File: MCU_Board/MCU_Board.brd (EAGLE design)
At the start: 88 x 41 mm, 81 parts, among them J1 22-05-7068-06, J10 22-05-7068-06, J11 22-05-7048-04, J12 22-27-2061-06, J13 USB3075-30-A, J14 22-05-7048-04, J15 1241050-5, J2 22-05-7068-06, J3 22-05-7028-02, J4 22-05-7028-02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

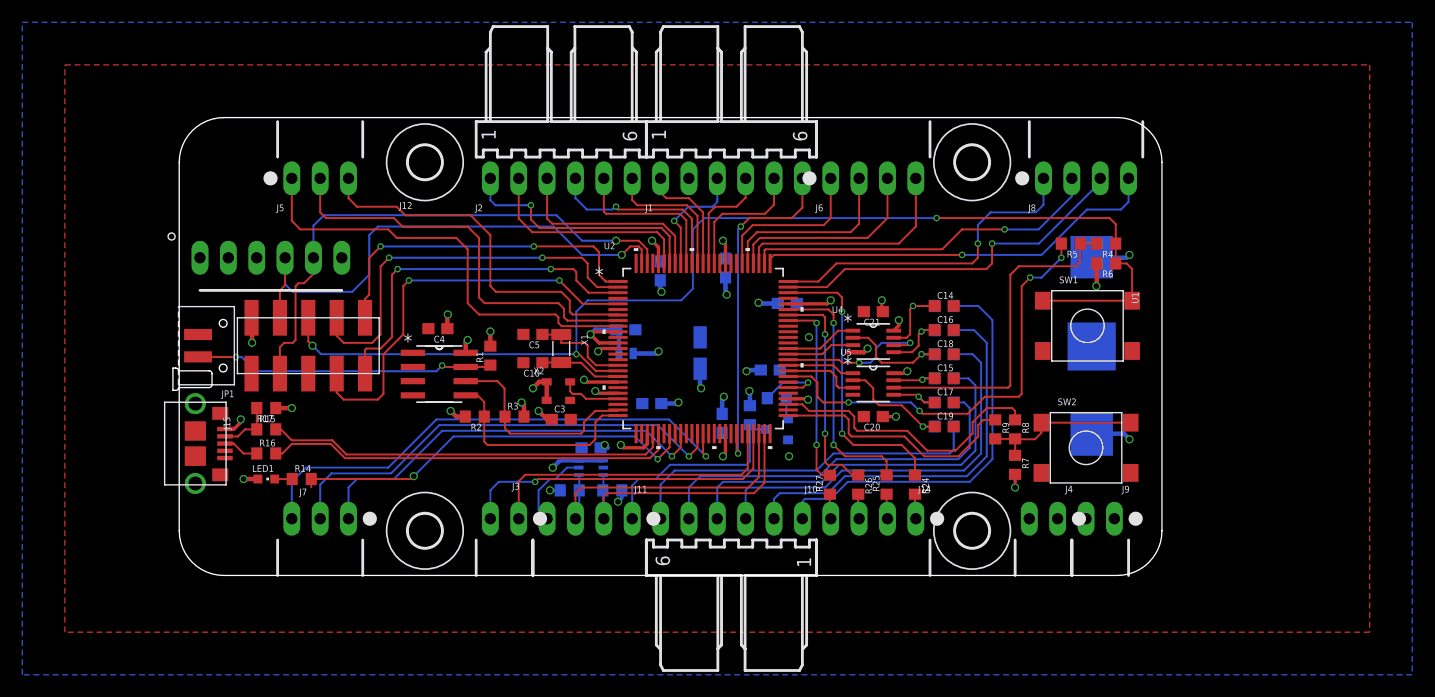
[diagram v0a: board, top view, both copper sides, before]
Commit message: Add limitation resistance on Encoder output, ADC input, relay input and fan Add LED on board Poly for +5V on Route15
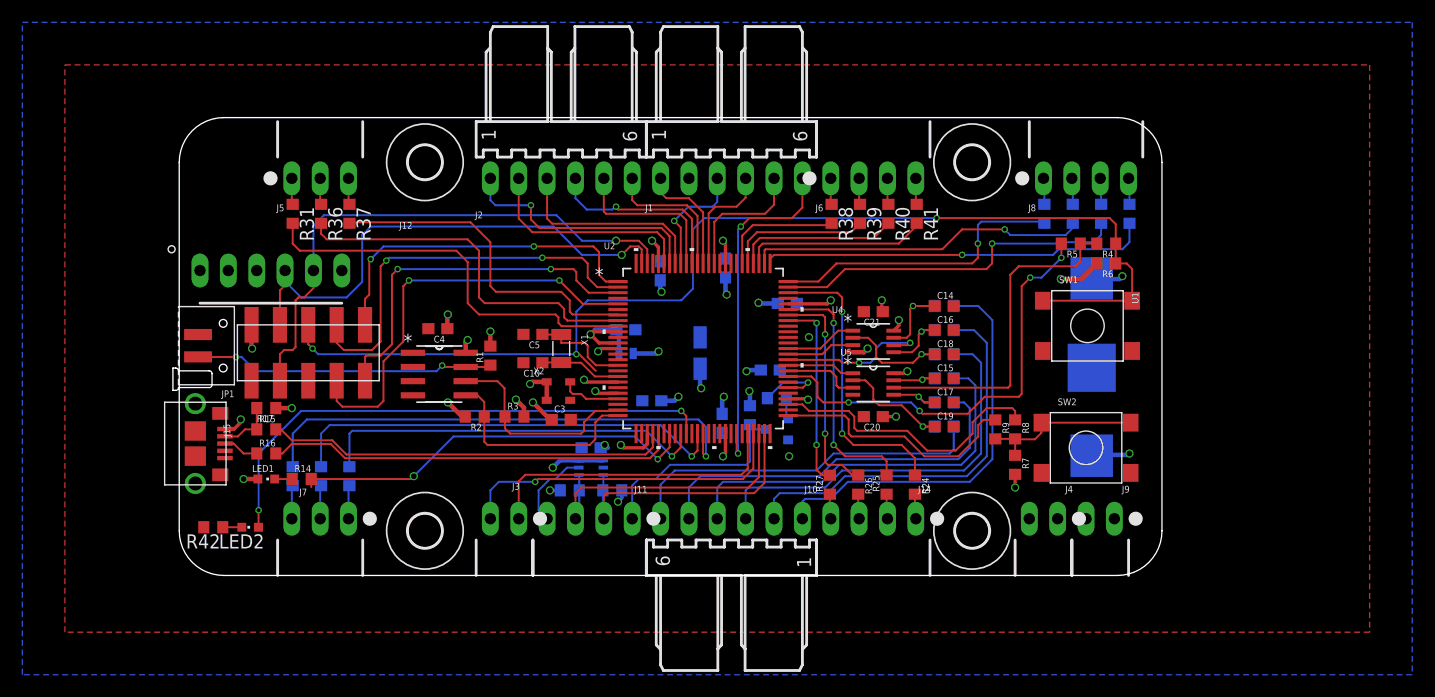
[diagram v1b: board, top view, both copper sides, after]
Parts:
- added LED2: (no value), led:CHIPLED_0603
- added R28, R29, R30, R31, R32, R33, R34, R35, R36, R37, R38, R39, R40, R41: 100, rcl:R0603
- added R42: 1K5, rcl:R0603
- moved X3 1.91 mm to (81.7, 18.6)
- moved J12 1.14 mm to (8.21, 27.3)
- moved J15 0.64 mm to (11.6, 19.9)
- moved C12 0.25 mm to (42.3, 15.6)
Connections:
- new net !RESET: U2.17
- new net LED_DEBUG: LED2.A, U2.35
- new net N$10: J8.3, R34.1
- new net N$11: J8.4, R35.1
- new net N$12: J5.3, R37.1
- new net N$13: J5.2, R36.1
- new net N$14: J5.1, R31.1
- new net N$21: J6.4, R41.1
- new net N$23: J6.3, R40.1
- new net N$24: J6.2, R39.1
- new net N$28: J6.1, R38.1
- new net N$29: LED2.C, R42.1
- new net N$3: J7.1, R28.1
- new net N$4: J7.2, R29.1
- new net N$6: J7.3, R30.1
- new net N$8: J8.1, R32.1
- new net N$9: J8.2, R33.1
- net ADC_SLACK_DETECTION: now also R37.2; no longer J5.3
- net ADC_TEMP_0: now also R31.2; no longer J5.1
- net ADC_TEMP_1: now also R36.2; no longer J5.2
- net BRAKE_SENSOR_1: now also R38.2; no longer J6.1
- net BRAKE_SENSOR_2: now also R39.2; no longer J6.2
- net DRIVE_EN: now also R40.2; no longer J6.3
- net DRIVE_ERR: now also R41.2; no longer J6.4
- net ENCODER_A: now also R28.2; no longer J7.1
- net ENCODER_B: now also R29.2; no longer J7.2
- net ENCODER_Z: now also R30.2; no longer J7.3
- net FAN_1_PWM: now also R32.2; no longer J8.1
- net FAN_1_SENSOR: now also R33.2; no longer J8.2
- net FAN_2_PWM: now also R34.2; no longer J8.3
- net FAN_2_SENSOR: now also R35.2; no longer J8.4
- net GND: now also R42.2
- net RESET: no longer U2.17
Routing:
- net +5V: track 74.7 -> 7.11 mm
- net LED_DEBUG: track 0.00 -> 48.3 mm, vias 0 -> 2
- net DRIVE_ERR: track 20.6 -> 16.6 mm
- net BRAKE_SENSOR_2: track 16.7 -> 12.7 mm
- net +3V3: track 57.0 -> 60.7 mm
- net DRIVE_EN: track 18.2 -> 14.6 mm
- net BRAKE_SENSOR_1: track 14.6 -> 11.0 mm
- net ADC_TEMP_1: track 37.3 -> 33.6 mm
- net ADC_TEMP_0: track 40.1 -> 36.9 mm
- net ADC_SLACK_DETECTION: track 33.5 -> 30.4 mm
- net N$6: track 0.00 -> 2.99 mm
- net N$4: track 0.00 -> 2.99 mm
- net N$3: track 0.00 -> 2.99 mm
- net FAN_1_PWM: track 29.8 -> 26.9 mm
- net RESET: track 105.9 -> 103.4 mm
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- added copper zone on layer 15, net +5V

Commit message: Add pin name on the board
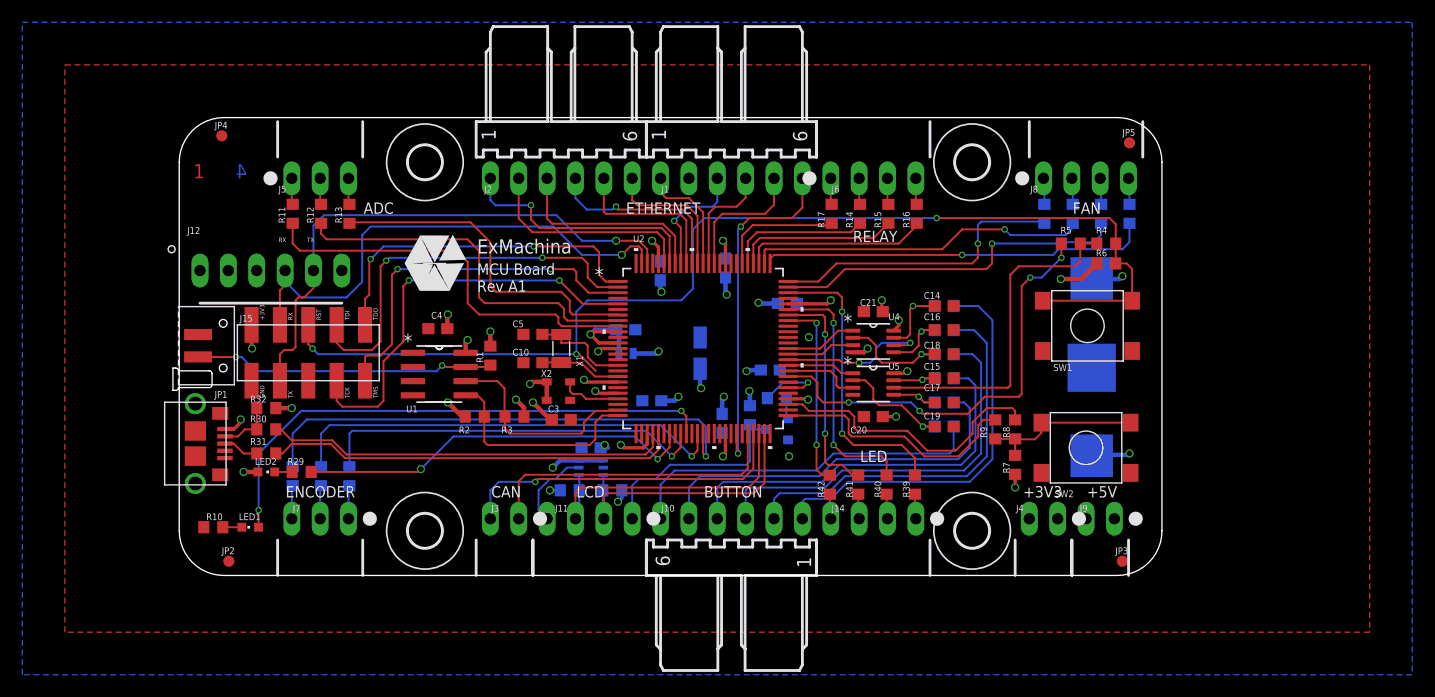
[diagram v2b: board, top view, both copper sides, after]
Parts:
- added JP2, JP3, JP4, JP5: FIDUCIAL1X2, SparkFun:FIDUCIAL-1X2
- added T2: EXMACHINA-LOGO-NAME, exmachina:EXM-LOGO-BASELINE
- LED1, LED2: value (none) -> Blue
- R10: value 4K7 -> 1K5
- R11, R15, R16: value 33 -> 100
- R12: value 4K7 -> 100
- R14, R17, R42: value 1K5 -> 100
- R18, R19, R20, R21, R22, R23: value 1K -> 100
- R25, R27: value 100 -> 4K7
- R26, R30, R31: value 100 -> 33
- R29, R32: value 100 -> 1K5
- R33, R34, R35, R36, R37, R38: value 100 -> 1K
- moved R32 71.8 mm to (7.79, 15.0), flipped to the top, turned to 180 degrees
- moved R16 62.1 mm to (66.0, 32.4), turned to 270 degrees
- moved R20 59.4 mm to (10.2, 8.89), turned to 90 degrees
- moved R15 59.0 mm to (63.5, 32.4), turned to 270 degrees
- moved R36 57.7 mm to (68.5, 17.7), flipped to the bottom, turned to 0 degrees
- moved R19 57.3 mm to (12.7, 8.89), turned to 90 degrees
- moved R37 55.9 mm to (68.5, 15.5), flipped to the bottom, turned to 0 degrees
- moved R18 55.4 mm to (15.2, 8.89), turned to 90 degrees
- moved R14 55.3 mm to (61.0, 32.4), turned to 270 degrees
- moved R42 55.3 mm to (58.3, 8.13), turned to 90 degrees
- moved R17 53.5 mm to (58.4, 32.4), turned to 270 degrees
- moved R11 44.7 mm to (10.2, 32.4), flipped to the top
- moved R13 41.7 mm to (15.2, 32.4), flipped to the top, turned to 270 degrees
- moved R28 38.9 mm to (53.5, 15.9), turned to 0 degrees
- moved R10 35.9 mm to (3.05, 4.32), flipped to the top, turned to 180 degrees
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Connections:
- net +3V3: now also LED2.A, R25.1, R27.1, R32.1; no longer LED1.A, R10.1, R12.1, R17.1
- net +5V: now also R26.1; no longer R11.1
- net ADC_SLACK_DETECTION: now also R13.2; no longer R37.2
- net ADC_TEMP_0: now also R11.2; no longer R31.2
- net ADC_TEMP_1: now also R12.2; no longer R36.2
- net BRAKE_SENSOR_1: now also R17.2; no longer R38.2
- net BRAKE_SENSOR_2: now also R14.2; no longer R39.2
- net DRIVE_EN: now also R15.2; no longer R40.2
- net DRIVE_ERR: now also R16.2; no longer R41.2
- net ENCODER_A: now also R18.2; no longer R28.2
- net ENCODER_B: now also R19.2; no longer R29.2
- net ENCODER_Z: now also R20.2; no longer R30.2
- net FAN_1_PWM: now also R21.2; no longer R32.2
- net FAN_1_SENSOR: now also R22.2; no longer R33.2
- net FAN_2_PWM: now also R23.2; no longer R34.2
- net FAN_2_SENSOR: now also R24.2; no longer R35.2
- net GND: now also R10.2; no longer R42.2
- net HMI_BUTTON_1: now also R33.1; no longer R18.1
- net HMI_BUTTON_2: now also R34.1; no longer R19.1
- net HMI_BUTTON_3: now also R35.1; no longer R20.1
- net HMI_BUTTON_4: now also R36.1; no longer R21.1
- net HMI_BUTTON_5: now also R37.1; no longer R22.1
- net HMI_BUTTON_6: now also R38.1; no longer R23.1
- net HMI_LCD_BACKLIGHT: now also R28.2; no longer R13.2
- net HMI_LCD_LED+: now also R26.2; no longer R11.2
- net HMI_LCD_SCL: now also R25.2; no longer R10.2
- net HMI_LCD_SDA: now also R27.2; no longer R12.2
- net HMI_LED_1: now also R39.1; no longer R24.1
- net HMI_LED_2: now also R40.2; no longer R25.2
- net HMI_LED_3: now also R41.1; no longer R26.1
- net HMI_LED_4: now also R42.2; no longer R27.2
- net LED_DEBUG: now also LED1.A; no longer LED2.A
- net N$1: now also R40.1; no longer R25.1
- net N$10: now also R23.1; no longer R34.1
- net N$11: now also R24.1; no longer R35.1
- net N$12: now also R13.1; no longer R37.1
- net N$13: now also R12.1; no longer R36.1
- net N$14: now also R11.1; no longer R31.1
- net N$15: now also R30.1, R32.2; no longer R15.1, R17.2
- net N$16: now also R31.1; no longer R16.1
- net N$17: now also R33.2; no longer R18.2
- net N$18: now also LED2.C, R29.1; no longer LED1.C, R14.1
- net N$19: now also R34.2; no longer R19.2
- net N$2: now also R42.1; no longer R27.1
- net N$20: now also R35.2; no longer R20.2
- net N$21: now also R16.1; no longer R41.1
- net N$23: now also R15.1; no longer R40.1
- net N$24: now also R14.1; no longer R39.1
- net N$25: now also R36.2; no longer R21.2
- net N$26: now also R37.2; no longer R22.2
- net N$27: now also R38.2; no longer R23.2
- net N$28: now also R17.1; no longer R38.1
- net N$29: now also LED1.C, R10.1; no longer LED2.C, R42.1
- net N$3: now also R18.1; no longer R28.1
- net N$4: now also R19.1; no longer R29.1
- net N$6: now also R20.1; no longer R30.1
- net N$63: now also R39.2; no longer R24.2
- net N$64: now also R41.2; no longer R26.2
- net N$7: now also R28.1; no longer R13.1
- net N$8: now also R21.1; no longer R32.1
- net N$9: now also R22.1; no longer R33.1
- net USB_D_N: now also R31.2; no longer R16.2
- net USB_D_P: now also R30.2; no longer R15.2
- net USB_UP_LED: now also R29.2; no longer R14.2
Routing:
- net USB_UP_LED: track 36.9 -> 35.9 mm
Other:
- board text added: "+3V3"
- board text added: "+5V"
- board text added: "1"
- board text added: "2"
- board text added: "3"
- board text added: "4"
- board text added: "ADC"
- board text added: "BUTTON"
- board text added: "CAN"
- board text added: "ENCODER"
- board text added: "ETHERNET"
- board text added: "FAN"
- board text added: "GND"
- board text added: "LCD"
- board text added: "LED"
- board text added: "MCU Board Rev A1"
- board text added: "RELAY"
- board text added: "RST"
- board text added: "RX"
- board text added: "TCK"
- board text added: "TDI"
- board text added: "TDO"
- board text added: "TMS"
- board text added: "TX"

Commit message: Generate gerber files and BOM and part list
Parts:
- J4: value 22-05-7028-02 -> 22-05-7038-03; device con-molex:7395-02 -> con-molex:7395-03
- moved J4 6.43 mm to (83.8, 5.08)
- moved J9 5.08 mm to (77.4, 5.08)
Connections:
- net +3V3: now also J4.2; no longer J4.1
- net AVDD: now also J4.1
- net GND: now also J4.3; no longer J4.2
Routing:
- net AVDD: track 10.0 -> 69.4 mm
- net VBAT+: track 82.6 -> 85.3 mm
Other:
- board size 88 x 41 mm -> 90 x 41.2 mm
